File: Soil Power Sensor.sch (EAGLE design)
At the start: 99 parts, among them J1 12401832E402A, U10 TPS7A20330PDBVR, U11 TPS60403DBVR, U12 REF1933AIDDCR, U13 TLV1117LV33DCYR, U14 FSA2466UMX, U2 FT234XD-R, U3 MAX9944ATA+T, U4 ESP32-C3-MINI-1-N4, U5 LTC6362CDDPBF, U6 LTC6362CDDPBF, U7 INA296A5, U8 MAX11201AEUB+, U9 MAX11201AEUB+, X1 SMA-142-0701-801/806

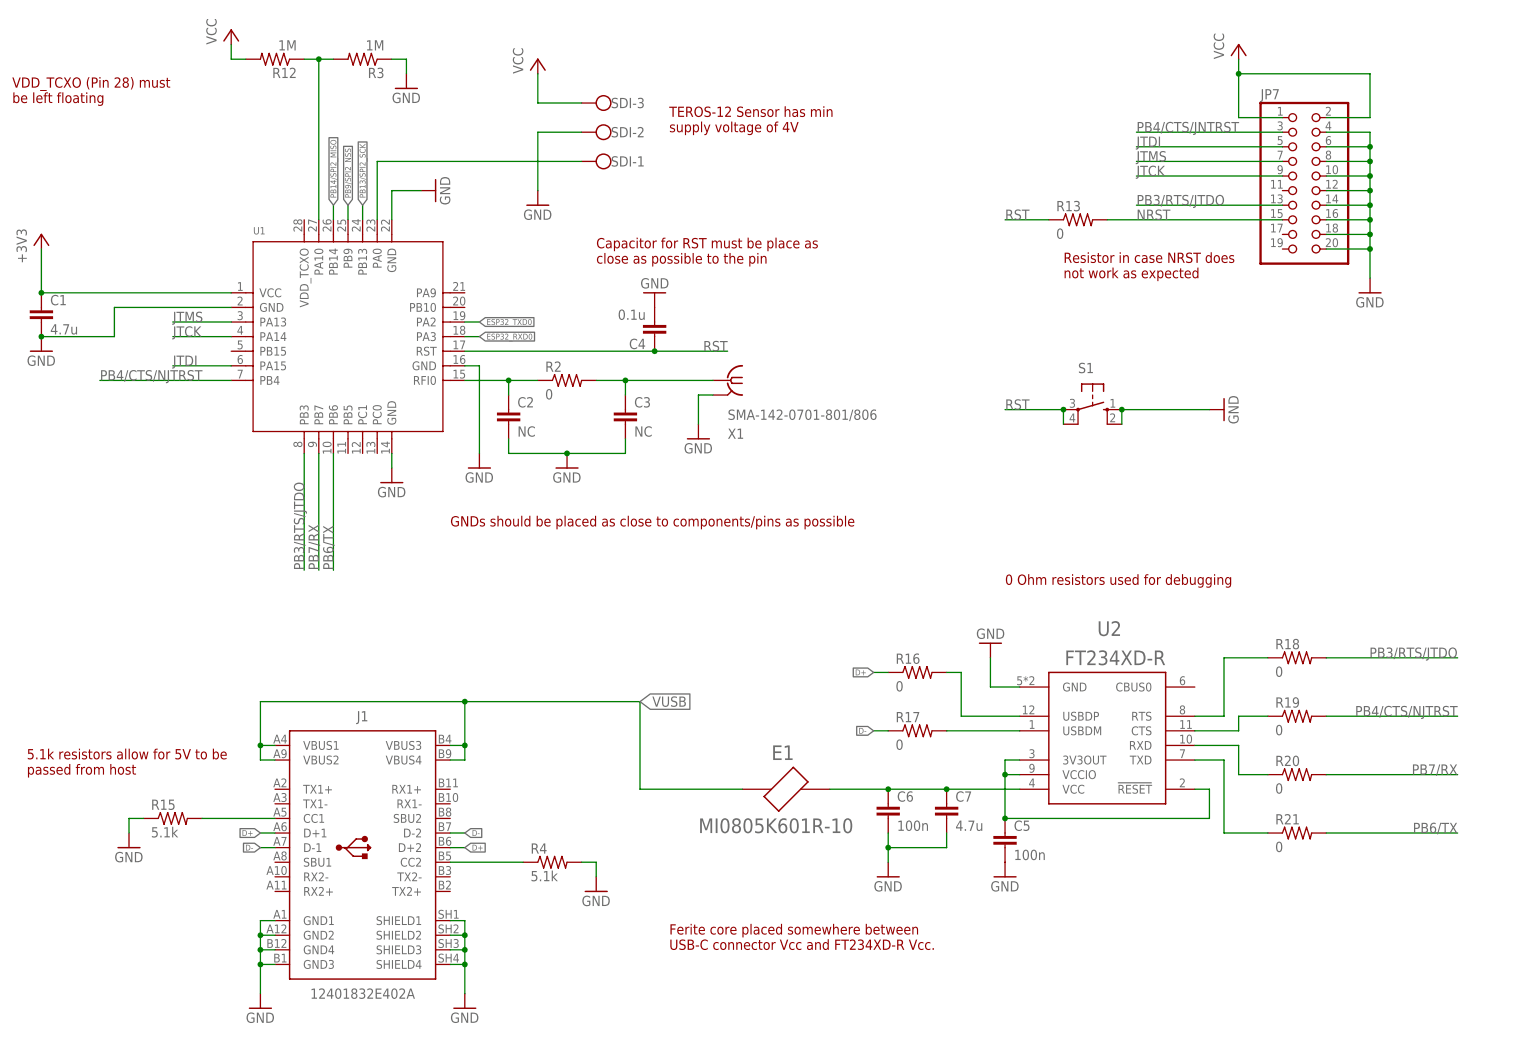
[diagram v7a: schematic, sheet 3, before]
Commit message: Added TVS diode on USB connector
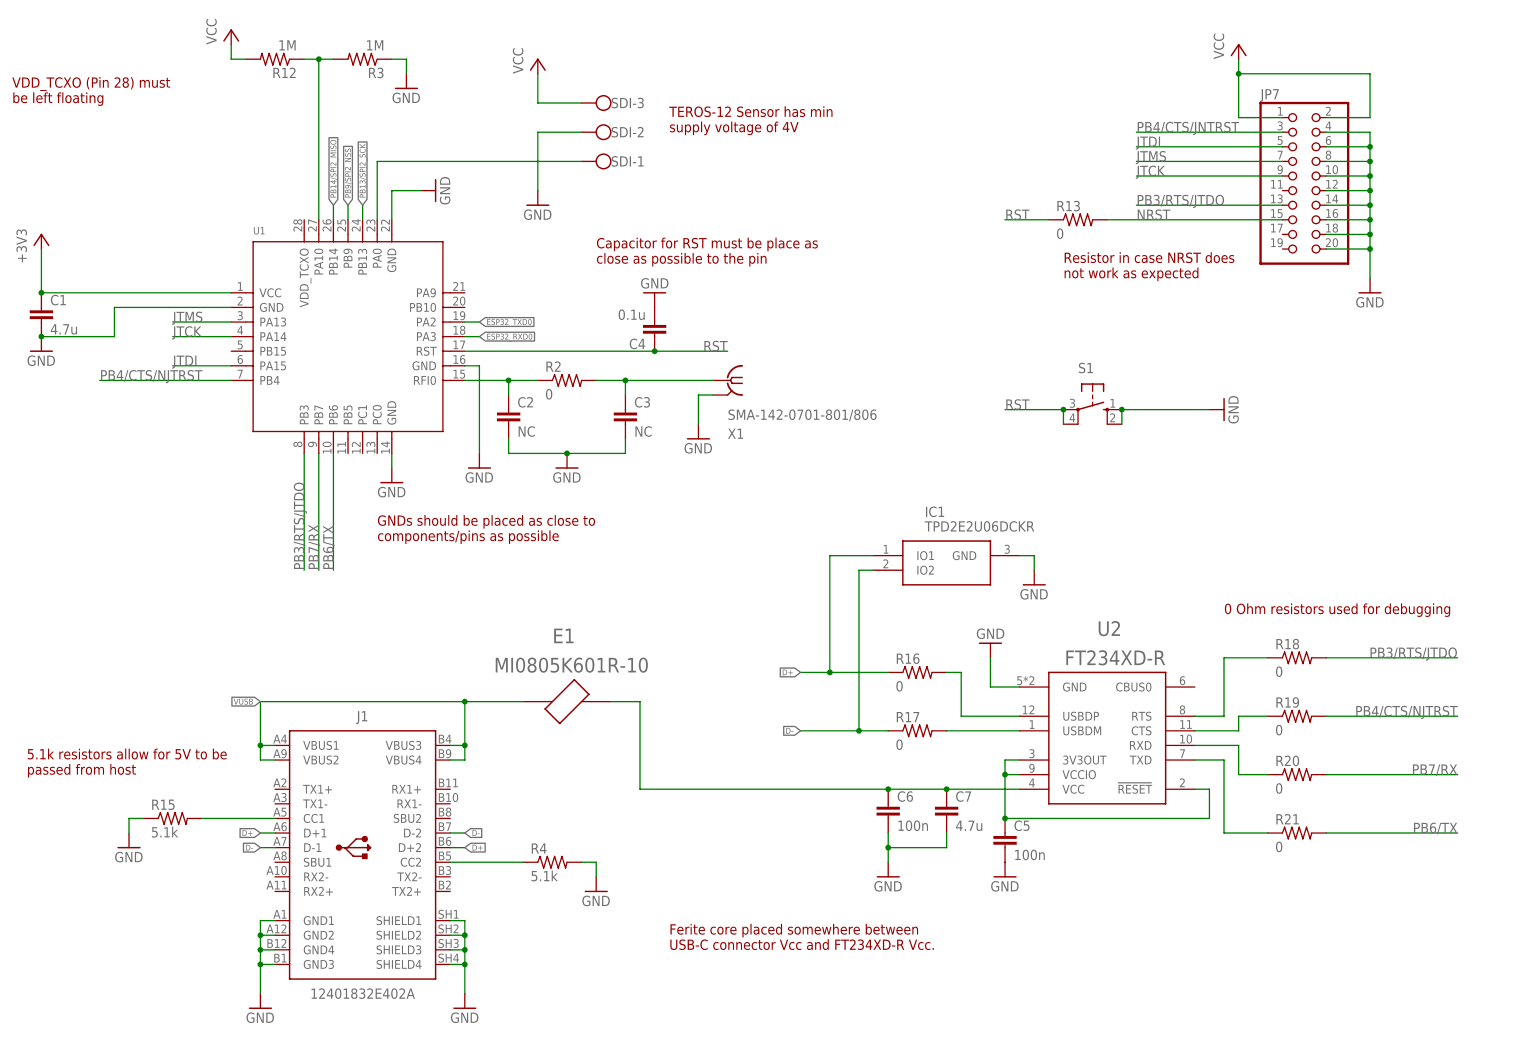
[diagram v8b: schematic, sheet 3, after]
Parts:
- added IC1: TPD2E2U06DCKR, Soil Power Sensor:TPD2E2U06DCKR
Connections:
- net D+: now also IC1.IO1
- net D-: now also IC1.IO2
- net GND: now also IC1.GND
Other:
- moved on the sheet: E1
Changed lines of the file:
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@@
 <part name="C7" library="rcl" library_urn="urn:adsk.eagle:library:334" deviceset="C-EU" device="C0603" package3d_urn="urn:adsk.eagle:package:23616/2" value="4.7u"/>
 <part name="GND16" library="supply1" library_urn="urn:adsk.eagle:library:371" deviceset="GND" device=""/>
-<part name="E1" library="Soil Power Sensor" deviceset="MI0805K601R-10" device=""/>
 <part name="G1" library="Soil Power Sensor" deviceset="AAA55" device=""/>
 <part name="G2" library="Soil Power Sensor" deviceset="AAA55" device=""/>
@@
 <part name="FRAME3" library="Soil Power Sensor" deviceset="FRAME_A_L" device="" value="STM32 and Digital Components"/>
 <part name="FRAME4" library="Soil Power Sensor" deviceset="FRAME_A_L" device="" value="WiFi and Bluetooth Module"/>
+<part name="IC1" library="Soil Power Sensor" deviceset="TPD2E2U06DCKR" device=""/>
+<part name="E1" library="Soil Power Sensor" deviceset="MI0805K601R-10" device=""/>
+<part name="GND43" library="supply1" library_urn="urn:adsk.eagle:library:371" deviceset="GND" device=""/>
 </parts>
 <sheets>
@@
 <text x="10.16" y="193.04" size="1.778" layer="94">VDD_TCXO (Pin 28) must
 be left floating</text>
-<text x="86.36" y="119.38" size="1.778" layer="94">GNDs should be placed as close to components/pins as possible</text>
+<text x="73.66" y="116.84" size="1.778" layer="94">GNDs should be placed as close to
+components/pins as possible</text>
 <text x="111.76" y="165.1" size="1.778" layer="94">Capacitor for RST must be place as
 close as possible to the pin</text>
-<text x="182.88" y="109.22" size="1.778" layer="94">0 Ohm resistors used for debugging</text>
+<text x="220.98" y="104.14" size="1.778" layer="94">0 Ohm resistors used for debugging</text>
 <text x="124.46" y="45.72" size="1.778" layer="94">Ferite core placed somewhere between
 USB-C connector Vcc and FT234XD-R Vcc.</text>
@@
 <attribute name="VALUE" x="160.02" y="55.88" size="1.778" layer="96"/>
 </instance>
-<instance part="E1" gate="G$1" x="144.78" y="73.66" smashed="yes">
-<attribute name="NAME" x="142.235559375" y="78.74148125" size="2.54148125" layer="95"/>
-<attribute name="VALUE" x="129.53003125" y="66.033359375" size="2.54331875" layer="96"/>
-</instance>
 <instance part="R3" gate="G$1" x="71.12" y="200.66" smashed="yes" rot="R180">
 <attribute name="NAME" x="74.93" y="199.1614" size="1.778" layer="95" rot="R180"/>
@@
 <attribute name="REVISION" x="251.46" y="7.62" size="2.54" layer="94"/>
 <attribute name="VALUE" x="173.99" y="6.604" size="2.54" layer="94"/>
+</instance>
+<instance part="IC1" gate="G$1" x="172.72" y="114.3" smashed="yes">
+<attribute name="NAME" x="168.91" y="121.92" size="1.778" layer="95" align="center-left"/>
+<attribute name="VALUE" x="168.91" y="119.38" size="1.778" layer="96" align="center-left"/>
+</instance>
+<instance part="E1" gate="G$1" x="106.68" y="88.9" smashed="yes">
+<attribute name="NAME" x="104.135559375" y="99.06148125" size="2.54148125" layer="95"/>
+<attribute name="VALUE" x="93.97003125" y="93.973359375" size="2.54331875" layer="96"/>
+</instance>
+<instance part="GND43" gate="1" x="187.96" y="109.22" smashed="yes">
+<attribute name="VALUE" x="185.42" y="106.68" size="1.778" layer="96"/>
 </instance>
 </instances>
@@
 <wire x1="109.22" y1="187.96" x2="101.6" y2="187.96" width="0.1524" layer="91"/>
 </segment>
+<segment>
+<pinref part="IC1" gate="G$1" pin="GND"/>
+<pinref part="GND43" gate="1" pin="GND"/>
+<wire x1="185.42" y1="114.3" x2="187.96" y2="114.3" width="0.1524" layer="91"/>
+<wire x1="187.96" y1="114.3" x2="187.96" y2="111.76" width="0.1524" layer="91"/>
+</segment>
 </net>
 <net name="N$2" class="0">
@@
 <segment>
 <pinref part="R16" gate="G$1" pin="1"/>
-<wire x1="162.56" y1="93.98" x2="160.02" y2="93.98" width="0.1524" layer="91"/>
-<label x="160.02" y="93.98" size="1.016" layer="95" rot="R180" xref="yes"/>
+<label x="147.32" y="93.98" size="1.016" layer="95" rot="R180" xref="yes"/>
+<wire x1="162.56" y1="93.98" x2="152.4" y2="93.98" width="0.1524" layer="91"/>
+<wire x1="152.4" y1="93.98" x2="147.32" y2="93.98" width="0.1524" layer="91"/>
+<pinref part="IC1" gate="G$1" pin="IO1"/>
+<wire x1="160.02" y1="114.3" x2="152.4" y2="114.3" width="0.1524" layer="91"/>
+<wire x1="152.4" y1="114.3" x2="152.4" y2="93.98" width="0.1524" layer="91"/>
+<junction x="152.4" y="93.98"/>
 </segment>
 <segment>
@@
 <segment>
 <pinref part="R17" gate="G$1" pin="1"/>
-<wire x1="162.56" y1="83.82" x2="160.02" y2="83.82" width="0.1524" layer="91"/>
-<label x="160.02" y="83.82" size="1.016" layer="95" rot="R180" xref="yes"/>
+<label x="147.32" y="83.82" size="1.016" layer="95" rot="R180" xref="yes"/>
+<wire x1="162.56" y1="83.82" x2="157.48" y2="83.82" width="0.1524" layer="91"/>
+<pinref part="IC1" gate="G$1" pin="IO2"/>
+<wire x1="157.48" y1="83.82" x2="147.32" y2="83.82" width="0.1524" layer="91"/>
+<wire x1="160.02" y1="111.76" x2="157.48" y2="111.76" width="0.1524" layer="91"/>
+<wire x1="157.48" y1="111.76" x2="157.48" y2="83.82" width="0.1524" layer="91"/>
+<junction x="157.48" y="83.82"/>
 </segment>
 <segment>
@@
 <segment>
 <pinref part="U2" gate="G$1" pin="VCC"/>
-<wire x1="152.4" y1="73.66" x2="162.56" y2="73.66" width="0.1524" layer="91"/>
 <wire x1="162.56" y1="73.66" x2="172.72" y2="73.66" width="0.1524" layer="91"/>
 <pinref part="C6" gate="G$1" pin="1"/>
@@
 <wire x1="172.72" y1="73.66" x2="185.42" y2="73.66" width="0.1524" layer="91"/>
 <junction x="172.72" y="73.66"/>
+<wire x1="114.3" y1="88.9" x2="119.38" y2="88.9" width="0.1524" layer="91"/>
+<wire x1="119.38" y1="88.9" x2="119.38" y2="73.66" width="0.1524" layer="91"/>
 <pinref part="E1" gate="G$1" pin="2"/>
+<wire x1="162.56" y1="73.66" x2="119.38" y2="73.66" width="0.1524" layer="91"/>
 </segment>
 </net>
@@
 <wire x1="88.9" y1="78.74" x2="88.9" y2="81.28" width="0.1524" layer="91"/>
 <junction x="88.9" y="81.28"/>
-<label x="119.38" y="88.9" size="1.778" layer="95" xref="yes"/>
-<wire x1="88.9" y1="88.9" x2="119.38" y2="88.9" width="0.1524" layer="91"/>
-<wire x1="119.38" y1="88.9" x2="119.38" y2="73.66" width="0.1524" layer="91"/>
 <junction x="88.9" y="88.9"/>
+<wire x1="88.9" y1="88.9" x2="99.06" y2="88.9" width="0.1524" layer="91"/>
 <pinref part="E1" gate="G$1" pin="1"/>
-<wire x1="119.38" y1="73.66" x2="137.16" y2="73.66" width="0.1524" layer="91"/>
-</segment>
-</net>
+<label x="53.34" y="88.9" size="1.016" layer="95" rot="R180" xref="yes"/>
+</segment>
+</net>
